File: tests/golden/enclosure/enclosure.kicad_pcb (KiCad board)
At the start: 2 copper layers, 48 x 34 mm, 11 parts, among them J1 USB_MICRO_B, J2 CONN_BRK_1X04, SW1 SW_TACT_SMD

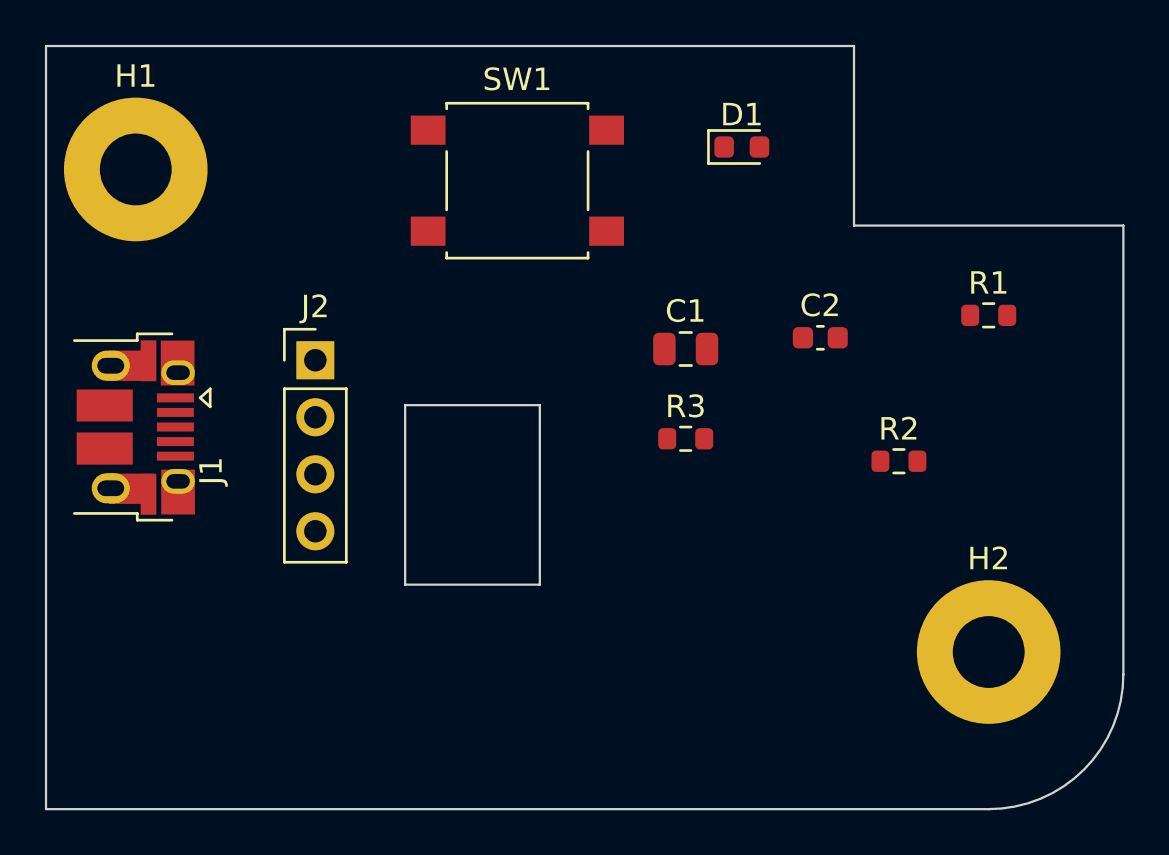
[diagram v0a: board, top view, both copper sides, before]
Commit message: M10: copper pours, stitching vias and plane integrity
Pours are source intent now: `pours:` says which net owns the free copper of
which layer, with priorities where two zones share one, thermal or solid pad
connection, per-pad-instance overrides, island-removal rules and a fragmentation
threshold. `stitching:` generates the vias that tie the pours together -- grid,
edge or ring -- as a deterministic pattern, in the architecture M9e established
for fanout escapes.

What aipcb emits is the zone and never the fill. KiCad's own engine produces the
copper, because KiCad's fill is what DRC checks against and a second
implementation would differ on every board (ADR 0009). `kicad-cli` 9.0.8 cannot
fill, so the engine is reached through a `pcbnew` subprocess with a version lock:
it refuses to fill unless pcbnew and kicad-cli report the same KiCad, and a fill
that fails is a check failure with pcbnew's stderr attached, never a quietly
unfilled board.

The split that makes this safe: `aipcb build` stays a byte-stable pure function
of the source with its zones unfilled, and `aipcb check` and `aipcb export` fill
a staged copy. An unfilled pour exports as no copper at all, silently, which is
why a failed fill stops the run instead of falling back.

After the fill, `aipcb check` reads the filled polygons back and reports what the
copper actually came out as -- islands, largest-island fraction, bounding boxes,
and what island removal deleted, measured by filling a second time with removal
off rather than inferred. `min_contiguous:` turns fragmentation into a warning
and never an error.

Eight of the ten examples gain a pour; `congestion` and `overconstrained` have no
ground net at all and keep none, which is also the live witness that a design
without `pours:` builds byte-identically. Four examples stitch. All ten pass
kicad-cli's DRC with zero violations on the board that was actually checked.

Three defects surfaced and are fixed: a stitching via drilled 0.21 mm from a
routed vi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
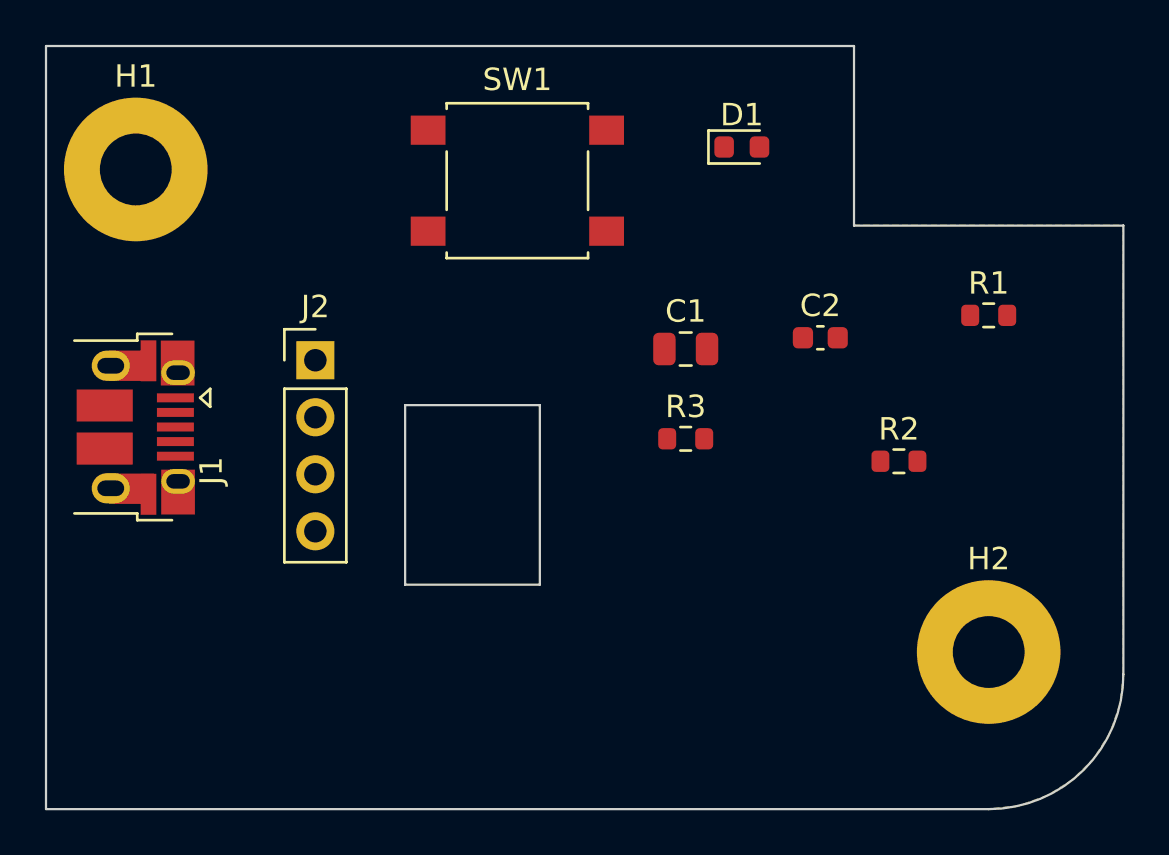
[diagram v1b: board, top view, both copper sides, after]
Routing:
- added copper zone on B.Cu, net GND
- added copper zone on F.Cu, net GND
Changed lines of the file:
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@@
 			(layers "F.Cu" "F.Mask" "F.Paste")
 			(net 2 "GND")
+			(zone_connect 2)
 		)
 		(pad "6" smd rect
@@
 			(layers "F.Cu" "F.Mask" "F.Paste")
 			(net 2 "GND")
+			(zone_connect 2)
 		)
 		(pad "6" smd rect
@@
 			(layers "F.Cu" "F.Mask" "F.Paste")
 			(net 2 "GND")
+			(zone_connect 2)
 		)
 		(pad "6" thru_hole oval
@@
 			(remove_unused_layers no)
 			(net 2 "GND")
+			(zone_connect 2)
 		)
 		(pad "6" thru_hole oval
@@
 			(remove_unused_layers no)
 			(net 2 "GND")
+			(zone_connect 2)
 		)
 		(pad "6" smd rect
@@
 			(layers "F.Cu" "F.Mask" "F.Paste")
 			(net 2 "GND")
+			(zone_connect 2)
 		)
 		(pad "6" smd rect
@@
 			(layers "F.Cu" "F.Mask" "F.Paste")
 			(net 2 "GND")
+			(zone_connect 2)
 		)
 		(pad "6" thru_hole oval
@@
 			(remove_unused_layers no)
 			(net 2 "GND")
+			(zone_connect 2)
 		)
 		(pad "6" thru_hole oval
@@
 			(remove_unused_layers no)
 			(net 2 "GND")
+			(zone_connect 2)
 		)
 		(pad "6" smd rect
@@
 			(layers "F.Cu" "F.Mask" "F.Paste")
 			(net 2 "GND")
+			(zone_connect 2)
 		)
 		(pad "6" smd rect
@@
 			(layers "F.Cu" "F.Mask" "F.Paste")
 			(net 2 "GND")
+			(zone_connect 2)
 		)
 		(pad "6" smd rect
@@
 			(layers "F.Cu" "F.Mask" "F.Paste")
 			(net 2 "GND")
+			(zone_connect 2)
 		)
 		(embedded_fonts no)
@@
 		(layer "Edge.Cuts")
 	)
+	(zone
+		(net 2)
+		(net_name "GND")
+		(layers "F.Cu" "B.Cu")
+		(hatch edge 0.5)
+		(connect_pads
+			(clearance 0.2)
+		)
+		(min_thickness 0.25)
+		(filled_areas_thickness no)
+		(fill yes
+			(thermal_gap 0.25)
+			(thermal_bridge_width 0.5)
+		)
+		(polygon
+			(pts
+				(xy 100 100)
+				(xy 136 100)
+				(xy 136 108)
+				(xy 148 108)
+				(xy 148 128)
+				(xy 147.849567 129.335126)
+				(xy 147.405813 130.603302)
+				(xy 146.690989 131.740939)
+				(xy 145.740939 132.690989)
+				(xy 144.603302 133.405813)
+				(xy 143.335126 133.849567)
+				(xy 142 134)
+				(xy 100 134)
+			)
+		)
+	)
 	(embedded_fonts no)
